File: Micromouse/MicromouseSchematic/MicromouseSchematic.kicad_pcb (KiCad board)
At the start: 2 copper layers, 155.7 x 131.7 mm, 105 parts, among them J1 Conn_01x06_MountingPin, J10 Conn_01x06_MountingPin, J11 Conn_01x07_Pin, J12 Conn_01x10, J13 Conn_01x06_Pin, J14 Conn_01x10, J2 Conn_01x06_MountingPin, J3 Conn_01x03_Pin, J4 Conn_01x02_Pin, J5 Conn_01x06_MountingPin, J6 IR_1, J7 IR_1, J8 IR_1, J9 IR_1, Q1 SFH300, Q10 DMN3065LW-7, Q2 DMN3065LW-7, Q3 SFH300, Q4 DMN3065LW-7, Q5 SFH300, Q6 DMN3065LW-7, Q9 SFH300, SW1 SW_Push, SW2 SW_Push, U1 VL53L1CXV0FY1, U11 MP6550GG-Z, U3 ICM-42688-P, U4 LIS2MDLTR, U5 STM32F746VETx, U7 MP6550GG-Z, Y1 8MHz, Y2 32.768kHz

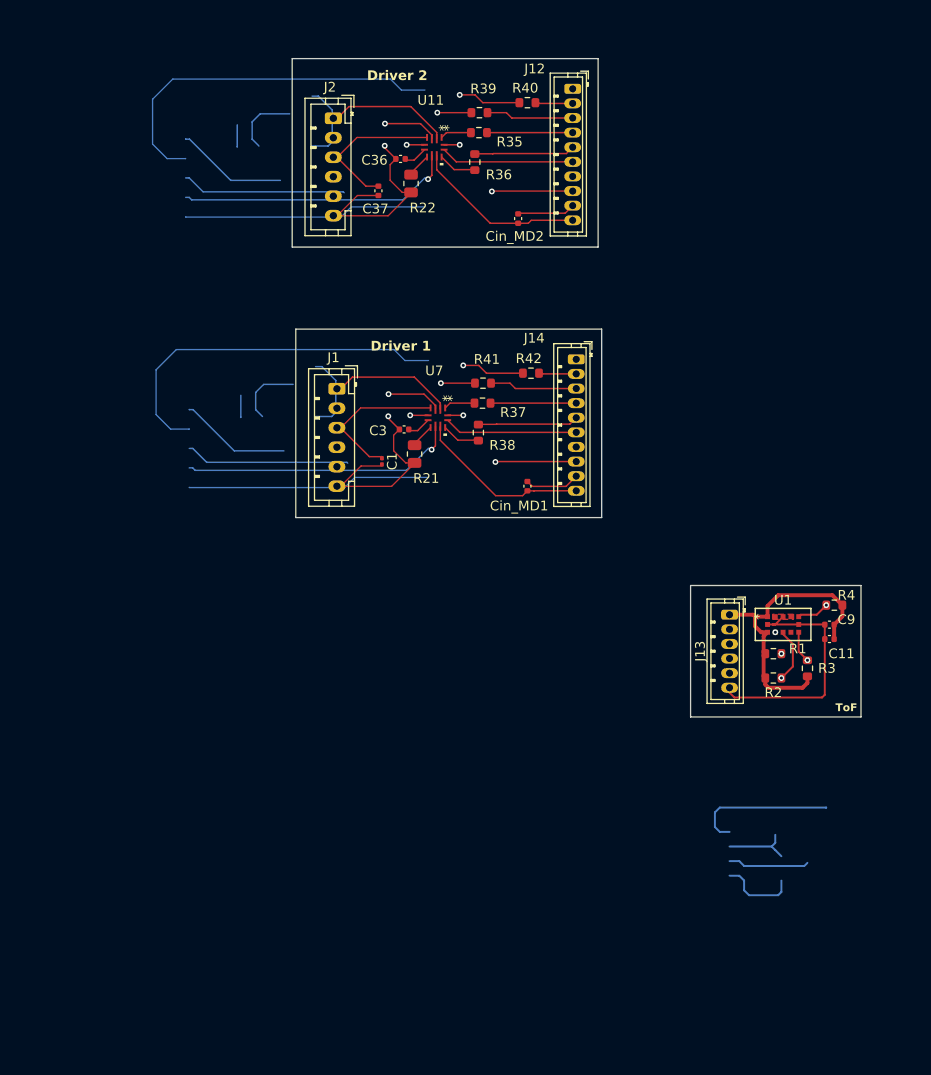
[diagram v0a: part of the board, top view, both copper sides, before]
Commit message: Fixed the rasnet issue and back copper layer issue
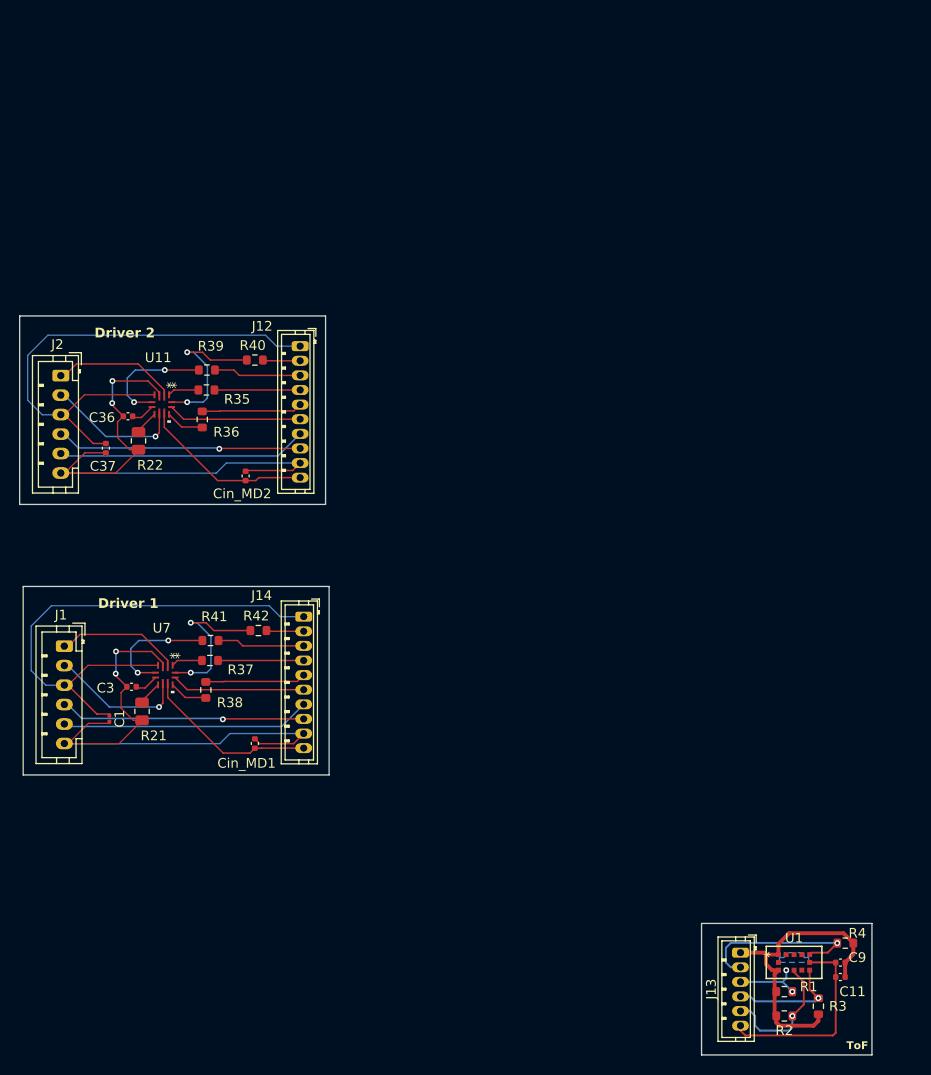
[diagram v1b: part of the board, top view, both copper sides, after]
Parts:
- moved Cin_MD1 38.5 mm to (54.8, 151.4)
- moved J14 38.5 mm to (59.8, 138.4)
- moved R37 38.5 mm to (50.1, 142.9)
- moved R40 38.5 mm to (54.8, 112.0)
- moved J1 38.5 mm to (35.2, 141.4)
- moved J2 38.5 mm to (34.8, 113.7)
- moved R36 38.5 mm to (49.4, 118.2)
- moved R38 38.5 mm to (49.7, 145.9)
- moved U7 38.5 mm to (45.6, 144.4)
- moved C1 38.5 mm to (39.8, 148.9)
- moved C3 38.5 mm to (42.1, 145.6)
- moved C36 38.5 mm to (41.7, 117.8)
- moved C37 38.5 mm to (39.5, 121.1)
- moved Cin_MD2 38.5 mm to (53.8, 124.0)
- moved J12 38.5 mm to (59.4, 110.6)
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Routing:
- net Net-(U11-NSLEEP_HB): track 24.4 -> 32.5 mm, vias 2 -> 4
- net NSLEEP_HB_1: track 6.46 -> 0.00 mm, vias 1 -> 0
- net GND: track 328.6 -> 324.5 mm
- net Net-(U7-NSLEEP_HB): track 1.60 -> 0.00 mm, vias 1 -> 0
- added copper zone on B.Cu, net GND
- removed copper zone on F.Cu, net GND
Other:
- board size 155.7 x 131.7 mm -> 179.5 x 166.4 mm

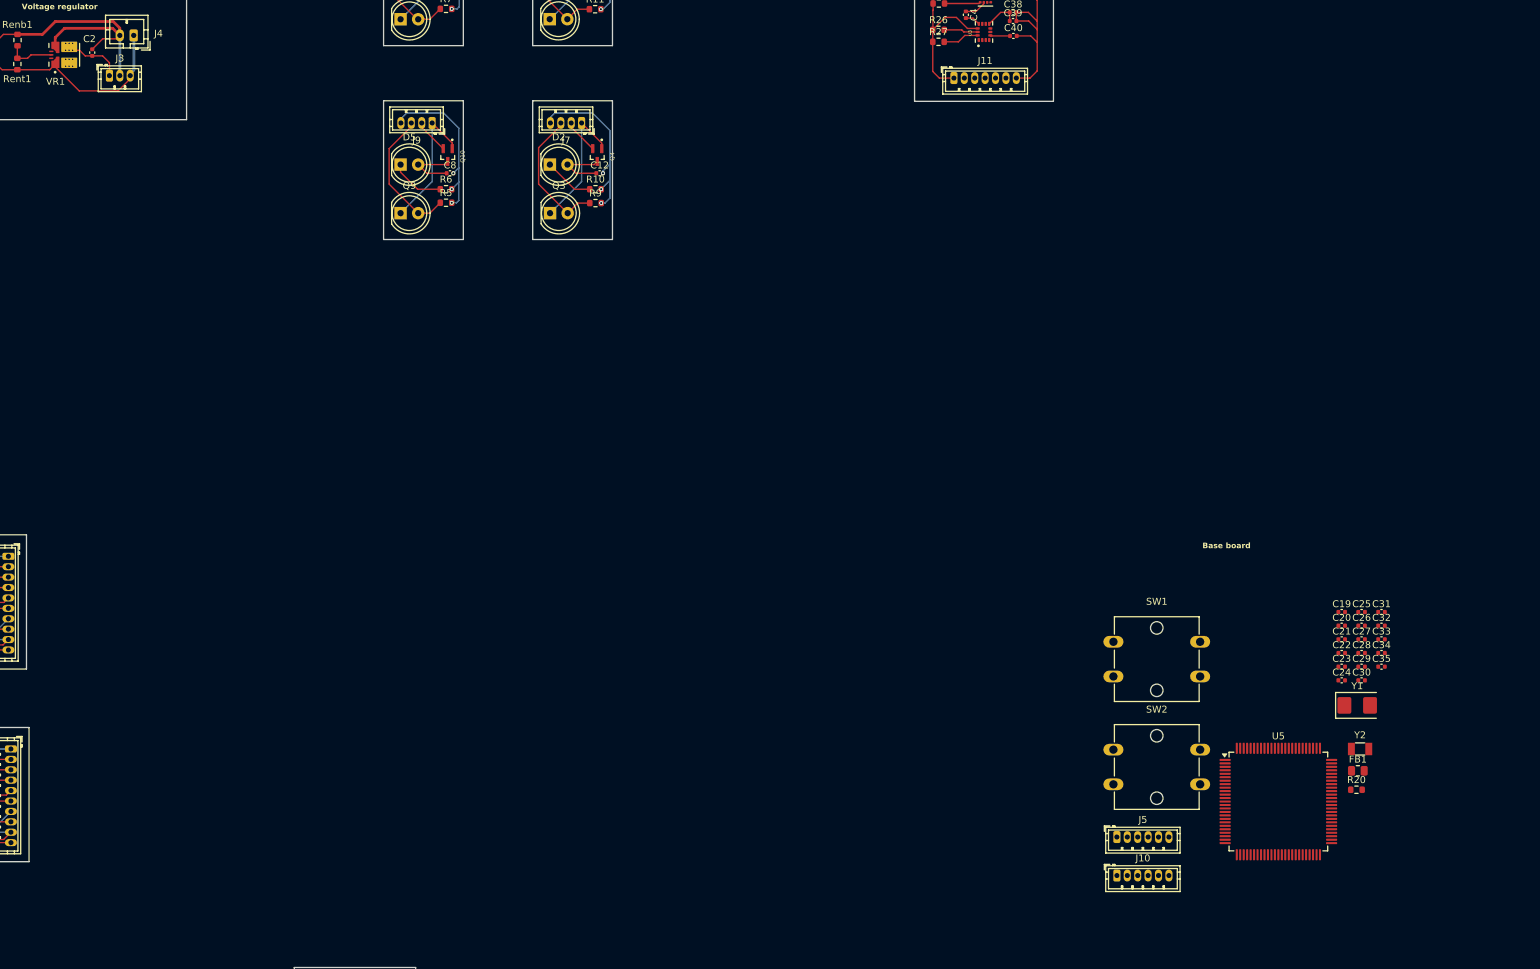
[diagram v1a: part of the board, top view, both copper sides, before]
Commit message: updated base pcd area, attached crystal oscillators and ferite bead -  must still figure out config for the connectors
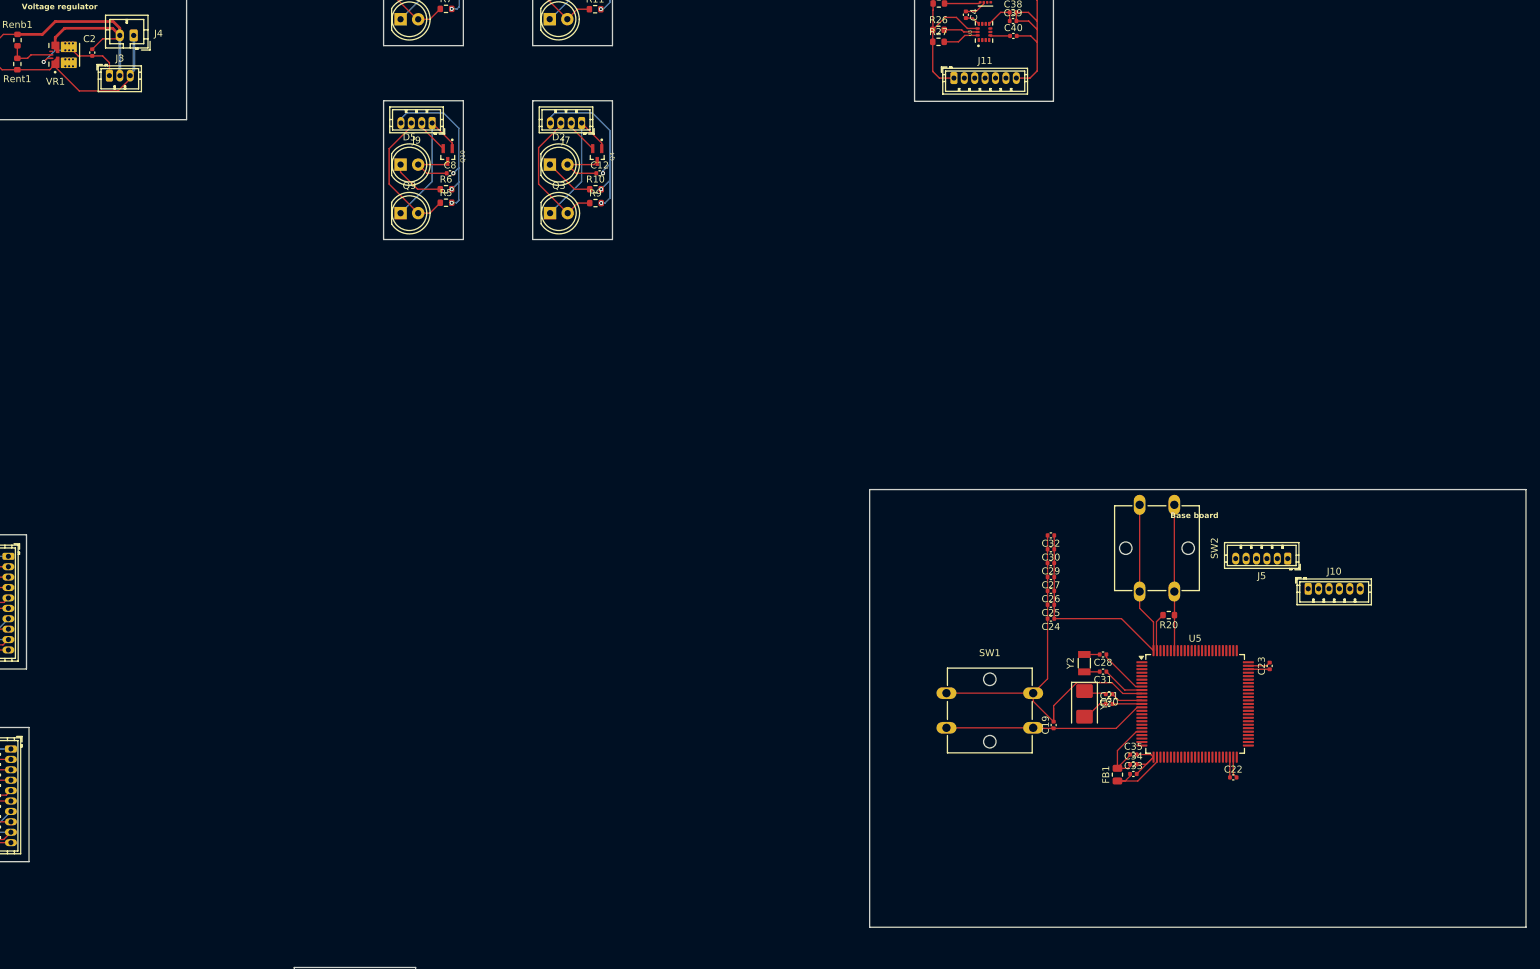
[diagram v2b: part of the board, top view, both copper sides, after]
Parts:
- moved J10 49.7 mm to (246.8, 115.3)
- moved C32 49.4 mm to (209.7, 107.6), turned to 180 degrees
- moved C30 48.6 mm to (209.7, 109.6), turned to 180 degrees
- moved C29 47.2 mm to (209.7, 111.6), turned to 180 degrees
- moved J5 47.1 mm to (243.8, 111.0), turned to 180 degrees
- moved C27 45.7 mm to (209.7, 113.6), turned to 180 degrees
- moved C26 45.1 mm to (209.7, 115.6), turned to 180 degrees
- moved C25 44.8 mm to (209.7, 117.6), turned to 180 degrees
- moved C19 44.6 mm to (210.1, 134.9), turned to 90 degrees
- moved C24 42.9 mm to (209.7, 119.6), turned to 180 degrees
- moved Y2 41.6 mm to (214.5, 126.0), turned to 90 degrees
- moved C31 41.1 mm to (217.2, 127.2), turned to 180 degrees
- moved C33 40.7 mm to (221.6, 142.0)
- moved Y1 39.3 mm to (214.6, 131.9), turned to -90 degrees
- moved C34 39.2 mm to (221.6, 140.6)
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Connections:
- VR1 pad 10: (no net) -> unconnected-(VR1-SW-Pad2)
- VR1 pad 11: (no net) -> unconnected-(VR1-SW-Pad2)
- VR1 pad 12: (no net) -> unconnected-(VR1-SW-Pad2)
- VR1 pad 13: (no net) -> unconnected-(VR1-SW-Pad2)
- VR1 pad 14: (no net) -> +3.3V
- VR1 pad 15: (no net) -> +3.3V
- VR1 pad 16: (no net) -> +3.3V
- VR1 pad 17: (no net) -> +3.3V
- VR1 pad 18: (no net) -> +3.3V
- VR1 pad 19: (no net) -> +3.3V
- VR1 pad 8: (no net) -> unconnected-(VR1-SW-Pad2)
- VR1 pad 9: (no net) -> unconnected-(VR1-SW-Pad2)
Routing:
- net GND: track 324.5 -> 406.4 mm
- net +3.3V: track 288.1 -> 353.4 mm, vias 0 -> 1
- net NRST: track 0.00 -> 29.8 mm
- net Net-(U5-BOOT0): track 0.00 -> 21.0 mm
- net 3V3A: track 0.00 -> 12.2 mm
- net Net-(U5-PC14): track 0.00 -> 7.27 mm
- net Net-(U5-PC15): track 0.00 -> 6.22 mm
- net Net-(U5-PH0): track 0.00 -> 4.62 mm
- net Net-(U5-PH1): track 0.00 -> 4.24 mm
- net Net-(C21-Pad1): track 0.00 -> 3.84 mm
- net Net-(C20-Pad2): track 0.00 -> 3.26 mm
- net Net-(U5-VCAP_2): track 0.00 -> 3.08 mm
- net Net-(U5-VCAP_1): track 0.00 -> 2.93 mm
- net Net-(C31-Pad2): track 0.00 -> 2.23 mm
- net Net-(C28-Pad2): track 0.00 -> 2.22 mm
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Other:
- board size 179.5 x 166.4 mm -> 247.6 x 166.4 mm
